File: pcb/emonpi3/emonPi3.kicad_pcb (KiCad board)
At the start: 4 copper layers, 85 x 88 mm, 182 parts, among them CN1 CONN_03SCREW, CN2 CONN_03SCREW, CN3 CONN_03SCREW, J1 SJ-3524-SMT-TR, J10 Conn_ARM_JTAG_SWD_10, J11 Conn_02x13_Odd_Even, J12 PINHD-1X9, J2 SJ-3524-SMT-TR, J3 SJ-3524-SMT-TR, J4 SJ-3524-SMT-TR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

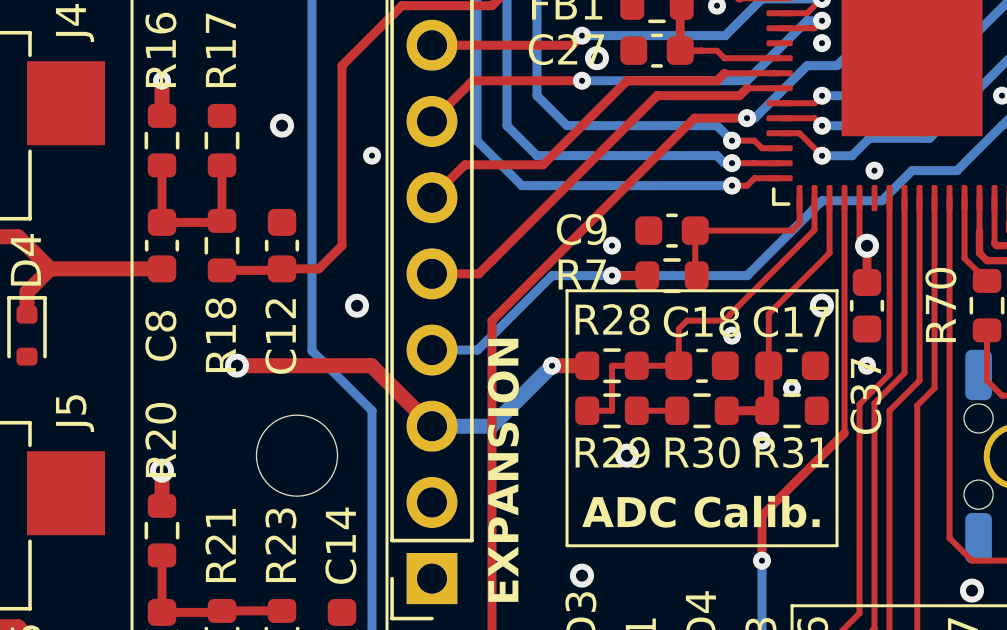
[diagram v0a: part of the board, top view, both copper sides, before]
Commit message: * Remove ANALOG_INPUT AA filter
  - Will be onboard expander board
  - Allows different use of the ANALOG_INPUT port
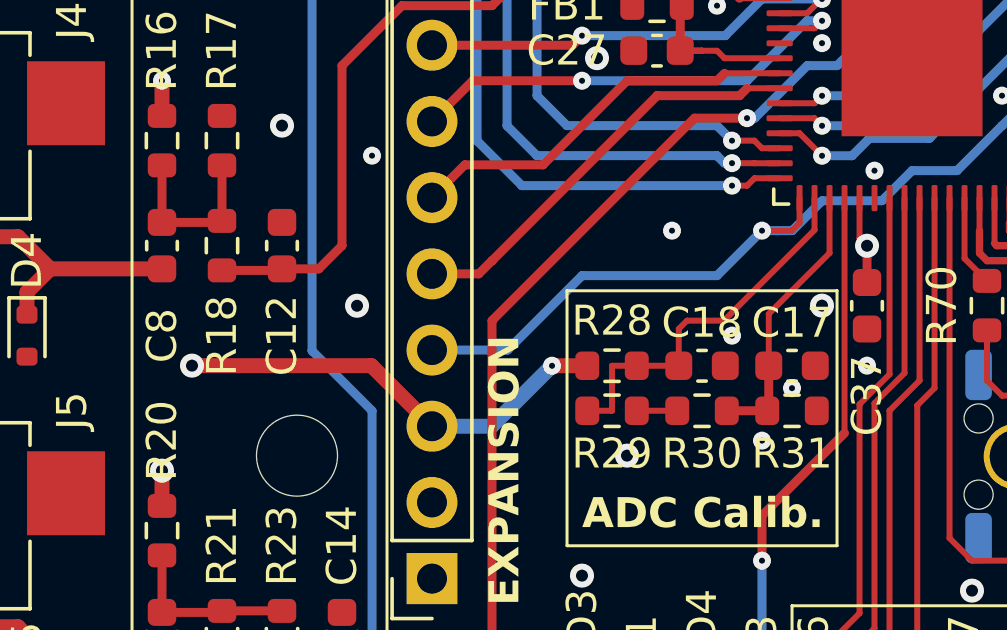
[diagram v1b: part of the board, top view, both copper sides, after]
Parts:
- removed C9: 10n, Capacitor_SMD:C_0603_1608Metric
- removed R7: 3K3, Resistor_SMD:R_0603_1608Metric
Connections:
- U3 pad 17: /AIN_LPFILT -> /ANALOG_INPUT
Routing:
- net /AIN_LPFILT: track 5.86 -> 0.00 mm
- net /ANALOG_INPUT: track 89.8 -> 90.8 mm

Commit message: * Split ANALOG_INPUT and CT12
  - Allows all 12 CTs to be used along with the ANALOG_INPUT
  - Removed USER LED0
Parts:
- removed LED3: Red 1.85V, LED_SMD:LED_0805_2012Metric
- removed R51: 1K, Resistor_SMD:R_0603_1608Metric
- U5: value ~ -> TPS2116
- U6: value MCP6456U -> MCP6546U
- U8: value 24AA02-OT -> 24FC08-OT
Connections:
- J12 pad 4: /ANALOG_INPUT -> /CT12
- U3 pad 17: /ANALOG_INPUT -> /CT12
- U3 pad 18: /VCAL_{HIGH} -> /ANALOG_INPUT
- U3 pad 19: /VCAL_{LOW} -> /VCAL_{HIGH}
- U3 pad 20: /~{USER_BUTTON} -> /VCAL_{LOW}
- U3 pad 23: /~{LED_USER0} -> /~{USER_BUTTON}
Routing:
- net /~{LED_USER0}: track 25.4 -> 0.00 mm
- net /ANALOG_INPUT: track 90.8 -> 75.7 mm
- net /CT12: track 0.00 -> 14.5 mm, vias 0 -> 1
- net /~{USER_BUTTON}: track 25.1 -> 32.5 mm, vias 2 -> 0
- net +3V3: track 161.3 -> 156.1 mm
- net Net-(LED3-A): track 2.49 -> 0.00 mm
- net /VCAL_{HIGH}: track 12.7 -> 13.4 mm
- net /UART_DBG_RX1: track 9.94 -> 10.5 mm
- net /VCAL_{LOW}: track 9.23 -> 9.79 mm
- net GND: vias 121 -> 123

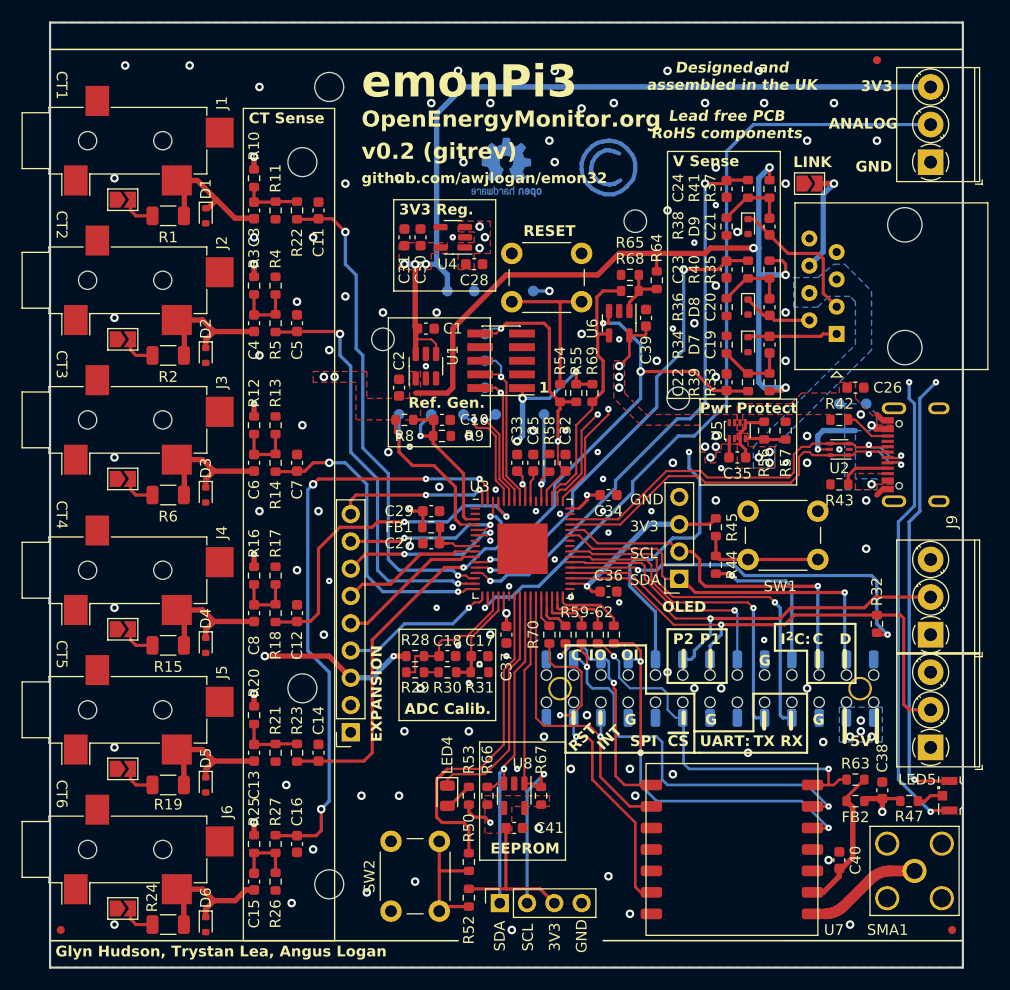
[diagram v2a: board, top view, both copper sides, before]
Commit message: * [ESD] Revise ESD protection strategy
  - All inputs and buttons have TVS and injection current limit
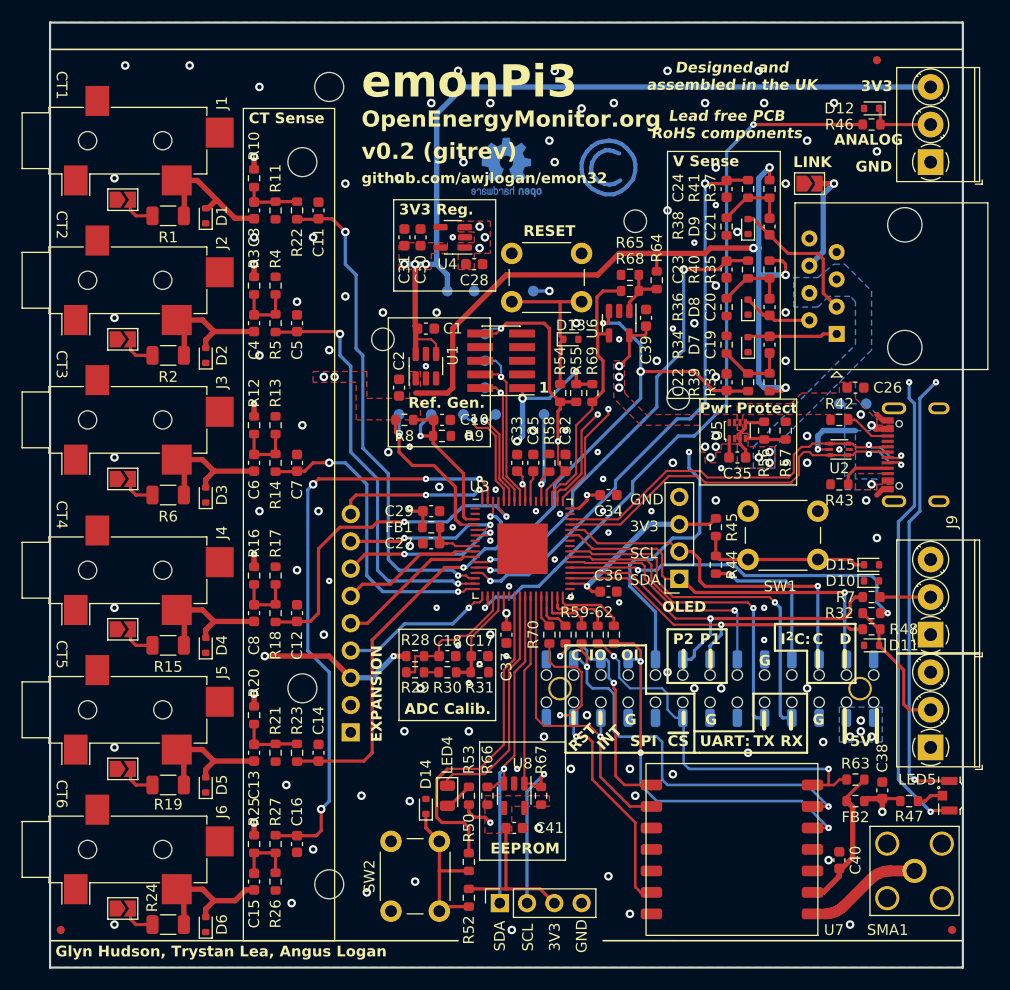
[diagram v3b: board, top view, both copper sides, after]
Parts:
- added D10: ESD5Z3.3T5G, Diode_SMD:D_SOD-523, F.Cu at (181.5, 114.0)
- added D11: ESD5Z3.3T5G, Diode_SMD:D_SOD-523, F.Cu at (181.5, 120.0)
- added D12: ESD5Z3.3T5G, Diode_SMD:D_SOD-523, F.Cu at (181.5, 70.0)
- added D13: ESD5Z3.3T5G, Diode_SMD:D_SOD-523, F.Cu at (153.5, 91.5)
- added D14: ESD5Z3.3T5G, Diode_SMD:D_SOD-523, F.Cu at (140.0, 135.0)
- added D15: ESD5Z3.3T5G, Diode_SMD:D_SOD-523, F.Cu at (181.5, 112.5)
- added R46: 1K, Resistor_SMD:R_0603_1608Metric, F.Cu at (181.5, 71.5)
- added R48: 1K, Resistor_SMD:R_0603_1608Metric, F.Cu at (181.5, 118.5)
- added R7: 1K, Resistor_SMD:R_0603_1608Metric, F.Cu at (181.5, 115.5)
- D1, D2, D3, D4, D5, D6, D7, D8, D9: value ESD -> 5V
- J12: moved to B.Cu
- moved R32 1.12 mm to (181.5, 117.0), turned to 180 degrees
- turned D1 to 90 degrees
- turned D2 to 90 degrees
- turned D3 to 90 degrees
- turned D4 to 90 degrees
- turned D5 to 90 degrees
- turned D6 to 90 degrees
- turned D7 to 90 degrees
- turned D8 to 90 degrees
- turned D9 to 90 degrees
- turned J12 to 0 degrees
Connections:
- C13 pad 1: Net-(D5-K) -> Net-(D5-A2)
- C15 pad 1: Net-(D6-K) -> Net-(D6-A2)
- C3 pad 1: Net-(D1-K) -> Net-(D1-A2)
- C4 pad 1: Net-(D2-K) -> Net-(D2-A2)
- C6 pad 1: Net-(D3-K) -> Net-(D3-A2)
- C8 pad 1: Net-(D4-K) -> Net-(D4-A2)
- CN1 pad 2: /PULSE2 -> Net-(CN1-Pin_2)
- CN2 pad 2: /P_OW_1 -> Net-(CN2-Pin_2)
- CN3 pad 2: /ANALOG_INPUT -> Net-(CN3-Pin_2)
- D1 pad 1: Net-(D1-K) -> GND
- D1 pad 2: GND -> Net-(D1-A2)
- D2 pad 1: Net-(D2-K) -> GND
- D2 pad 2: GND -> Net-(D2-A2)
- D3 pad 1: Net-(D3-K) -> GND
- D3 pad 2: GND -> Net-(D3-A2)
- D4 pad 1: Net-(D4-K) -> GND
- D4 pad 2: GND -> Net-(D4-A2)
- D5 pad 1: Net-(D5-K) -> GND
- D5 pad 2: GND -> Net-(D5-A2)
- D6 pad 1: Net-(D6-K) -> GND
- D6 pad 2: GND -> Net-(D6-A2)
- D7 pad 1: /VS1 -> GND
- D7 pad 2: GND -> /VS1
- D8 pad 1: /VS2 -> GND
- D8 pad 2: GND -> /VS2
- D9 pad 1: /VS3 -> GND
- D9 pad 2: GND -> /VS3
- J1 pad T: Net-(D1-K) -> Net-(D1-A2)
- J2 pad T: Net-(D2-K) -> Net-(D2-A2)
- J3 pad T: Net-(D3-K) -> Net-(D3-A2)
- J4 pad T: Net-(D4-K) -> Net-(D4-A2)
- J5 pad T: Net-(D5-K) -> Net-(D5-A2)
- J6 pad T: Net-(D6-K) -> Net-(D6-A2)
- R1 pad 1: Net-(D1-K) -> Net-(D1-A2)
- R15 pad 1: Net-(D4-K) -> Net-(D4-A2)
- R19 pad 1: Net-(D5-K) -> Net-(D5-A2)
- R2 pad 1: Net-(D2-K) -> Net-(D2-A2)
- R24 pad 1: Net-(D6-K) -> Net-(D6-A2)
- R32 pad 2: /P_OW_1 -> Net-(CN2-Pin_2)
- R6 pad 1: Net-(D3-K) -> Net-(D3-A2)
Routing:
- net /P_OW_1: track 47.8 -> 32.9 mm
- net Net-(CN2-Pin_2): track 0.00 -> 12.7 mm
- net Net-(D1-K): track 12.5 -> 0.00 mm
- net Net-(D1-A2): track 0.00 -> 12.5 mm
- net Net-(D6-K): track 12.5 -> 0.00 mm
- net Net-(D6-A2): track 0.00 -> 12.5 mm
- net Net-(D5-K): track 12.1 -> 0.00 mm
- net Net-(D5-A2): track 0.00 -> 12.1 mm
- net Net-(D4-K): track 12.0 -> 0.00 mm
- net Net-(D4-A2): track 0.00 -> 12.0 mm
- net Net-(D3-K): track 12.0 -> 0.00 mm
- net Net-(D3-A2): track 0.00 -> 12.0 mm
- net Net-(D2-K): track 12.0 -> 0.00 mm
- net Net-(D2-A2): track 0.00 -> 12.0 mm
- net /ANALOG_INPUT: track 75.7 -> 69.4 mm, vias 1 -> 2
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
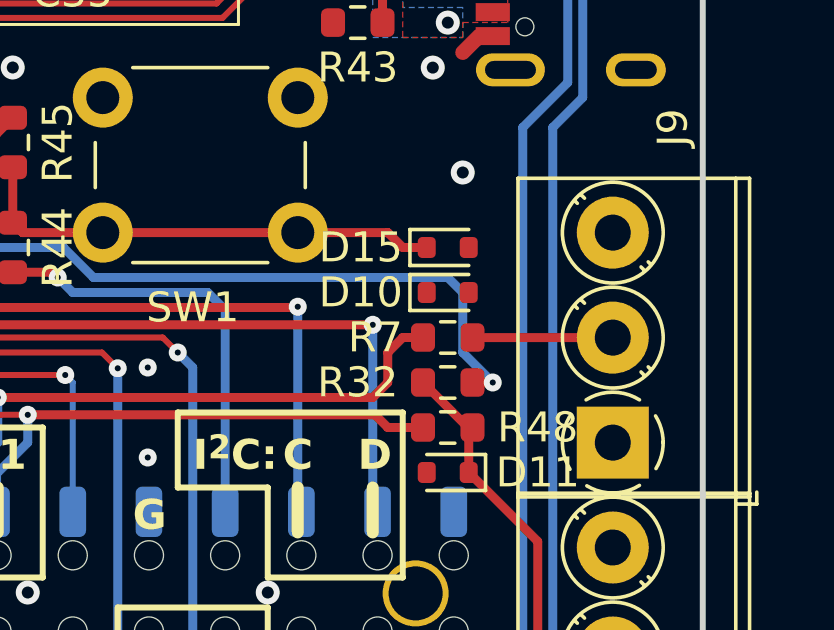
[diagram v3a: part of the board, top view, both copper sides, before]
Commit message: * Add missing trace
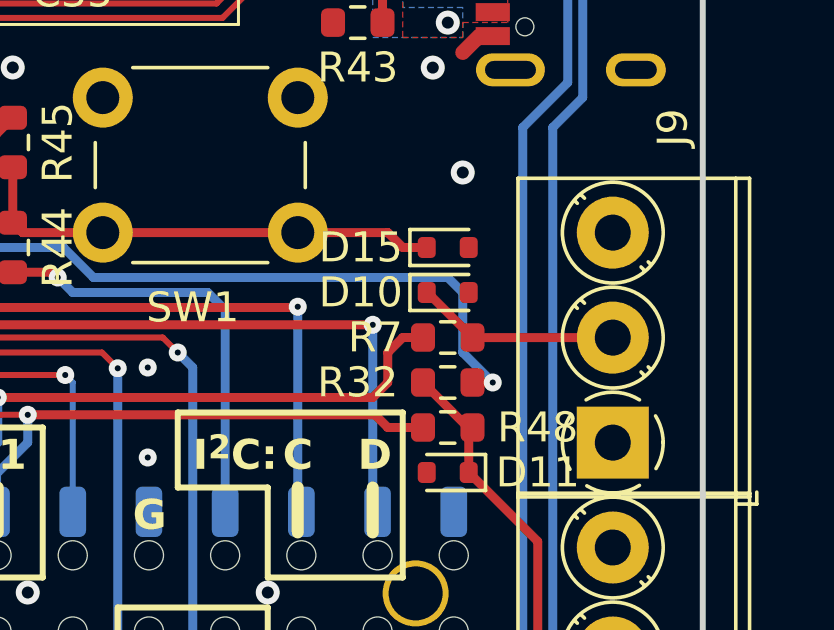
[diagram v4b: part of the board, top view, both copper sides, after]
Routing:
- net Net-(CN1-Pin_2): track 4.67 -> 6.82 mm
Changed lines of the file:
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@@
   (footprint "valcon-usb:CSP-USC16-TR" locked (layer "F.Cu")
     (at 186.5011 102.0036 90)
+    (property "Alternate" "Amphenol 12402012E212A ")
     (property "Sheetfile" "emonPi3.kicad_sch")
     (property "Sheetname" "")
@@
     (property "Sheetfile" "emonPi3.kicad_sch")
     (property "Sheetname" "")
+    (property "dnp" "")
     (property "ki_description" "ESD Protection Diode, SOD-523")
     (property "ki_keywords" "esd tvs unidirectional diode")
@@
   (segment (start 146.8811 133.5) (end 146.8811 144.0036) (width 0.3) (layer "B.Cu") (net 75))
   (segment (start 146.8811 133.5) (end 146.8811 131.895) (width 0.3) (layer "B.Cu") (net 75))
+  (segment (start 182.325 115.5) (end 180.825 114) (width 0.3) (layer "F.Cu") (net 76))
+  (segment (start 180.825 114) (end 180.8 114) (width 0.2) (layer "F.Cu") (net 76))
   (segment (start 187.0011 115.5036) (end 182.3286 115.5036) (width 0.3) (layer "F.Cu") (net 76))
   (segment (start 155.5 111) (end 155.5 111.0036) (width 0.2) (layer "F.Cu") (net 77))
